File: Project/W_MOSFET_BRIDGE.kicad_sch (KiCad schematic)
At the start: 14 parts, among them Q501 DMT68M8LFV-7, Q502 DMT68M8LFV-7

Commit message: More files cleanup
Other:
- company: Quasi Peak -> ${COMPANY}

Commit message: Cleanup ED A1 version
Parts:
- C503: symbol Device:CP -> Device:C_Polarized
- Q501, Q502: symbol eval_board_tmc6200-ta:DMT68M8LFV-7 -> QP_LIBRARY:DMT68M8LFV-7

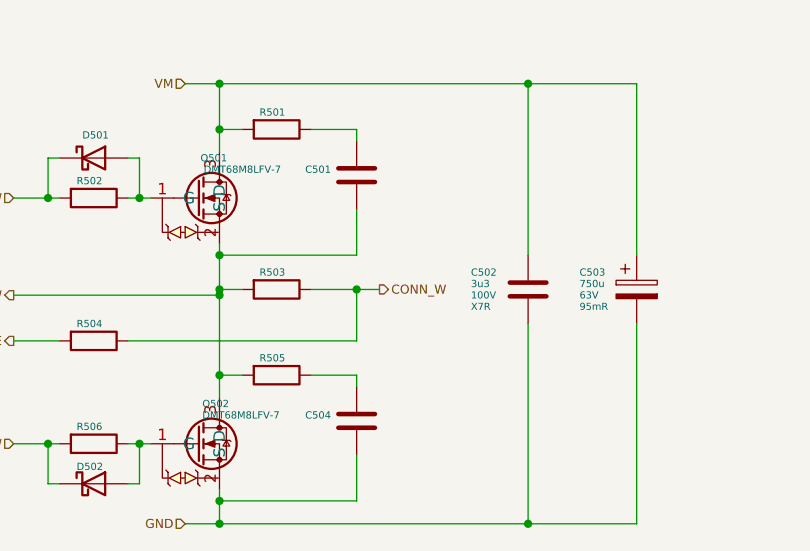
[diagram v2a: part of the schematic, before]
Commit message: Cleaning files, added testpoints
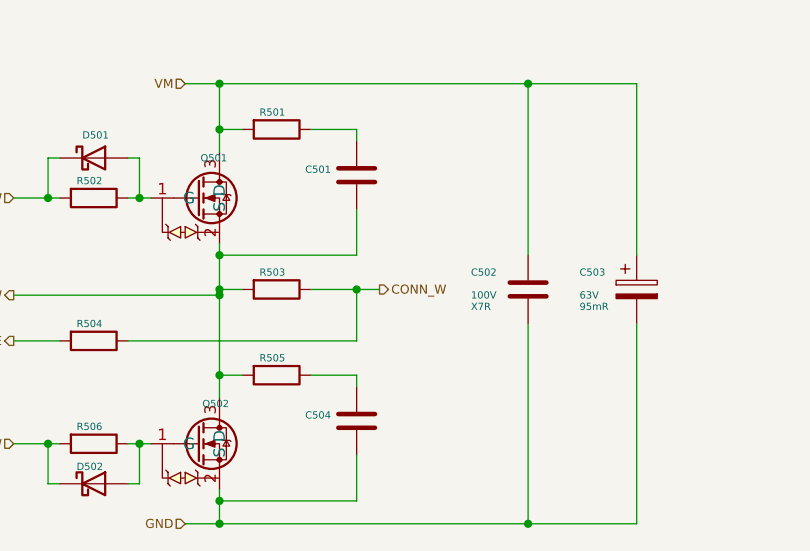
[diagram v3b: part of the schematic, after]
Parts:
- C501, C504: value C -> ~; footprint Capacitor_SMD:C_0402_1005Metric -> (none)
- C502: value 3u3 -> ~; footprint Capacitor_SMD:C_1812_4532Metric -> (none)
- C503: value 750u -> ~; footprint Capacitor_SMD:CP_Elec_18x17.5 -> (none)
- D501, D502: value D_Schottky -> ~; footprint Diode_SMD:D_SOD-123 -> (none)
- Q501, Q502: value DMT68M8LFV-7 -> ~; footprint eval_board_tmc6200-ta:DMT68M8LFV-7_PowerDI5060-8 -> (none)
- R501, R502, R504, R505, R506: value R -> ~; footprint Resistor_SMD:R_0402_1005Metric -> (none)
- R503: value R -> ~; footprint Resistor_SMD:R_1210_3225Metric -> (none)
